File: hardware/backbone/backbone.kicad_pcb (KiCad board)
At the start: 4 copper layers, 31.3 x 68.9 mm, 113 parts, among them J1 RESET, J10 CORE_A, J11 MOUNT, J12 PW, J13 FIELD_B, J14 FIELD_A, J15 UART PROG, J16 ALED, J2 FROM_PREVIOUS, J4 FROM_PREVIOUS, J5 CONN_A, J6 BOOTLOADER, J7 CONN_B, J8 CORE_B, J9 TO NEXT, Q2 AO3401A, U11 470nH DCR=450m, U13 470nH DCR=450m, U15 ST25R100, U17 BLM18PG471SZ1D, U2 SN65HVD230DR, U4 AP2112K-3.3TRG1, U5 ESP32-C3-MINI-1-H4X, U8 G3VM-61VY3, U9 SN74AHCT1G14DCKR, X1 NX2016SA 27.12MHz

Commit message: fixed silkscreen
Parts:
- removed kobee-studio-6AA93B92: Kobee Studio, kobee-studio-6AA82ECF
- added kobee-studio-6AAAAB89: Kobee Studio, kobee-studio-6AA835EE, F.Cu at (177.9, 83.1)
- added kobee-studio-6AAAAB9F: Kobee Studio, kobee-studio-6AA835EE, F.Cu at (173.6, 83.5)
- moved kobee-studio-6AA93B19 17.8 mm to (167.4, 105.8), turned to 0 degrees
- moved kobee-studio-6AA93BB9 4.59 mm to (176.9, 123.6), turned to 90 degrees
- moved kobee-studio-6AAAAAAB 0.76 mm to (178.8, 112.3)
- moved kobee-studio-6AAAAAA1 0.41 mm to (178.8, 109.5)
- moved kobee-studio-6AAAAB45 0.27 mm to (156.4, 112.3)
- moved kobee-studio-6AA93B26 0.20 mm to (180.9, 88.0)
- moved kobee-studio-6AAAAA98 0.17 mm to (178.8, 106.7)
- moved kobee-studio-6AAAAB56 0.07 mm to (156.4, 109.2)
- renumbered kobee-studio-6AA83BBD to kobee-studio-6AAAAA98, kobee-studio-6AA83BE1 to kobee-studio-6AAAAAA1, kobee-studio-6AA83B6C to kobee-studio-6AAAAAAB, kobee-studio-6AA83B6C to kobee-studio-6AAAAB45, kobee-studio-6AA83B72 to kobee-studio-6AAAAB56

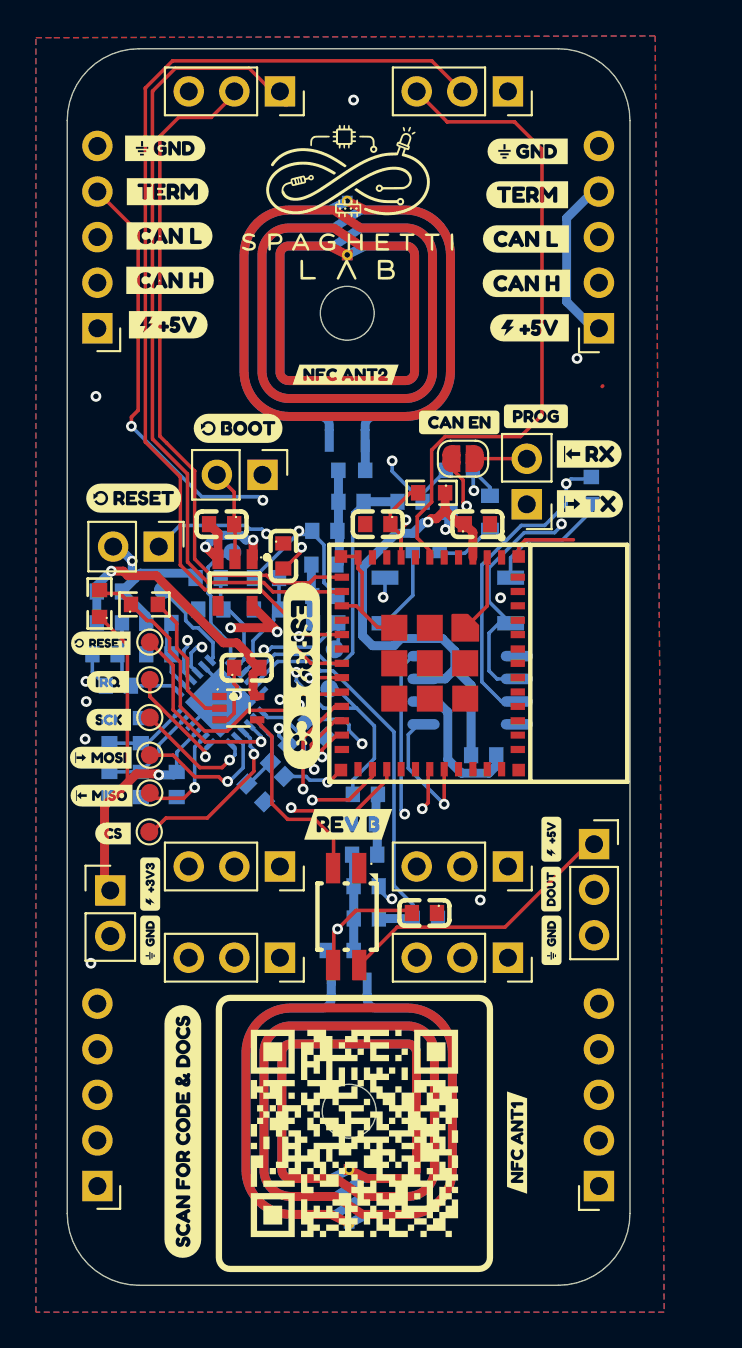
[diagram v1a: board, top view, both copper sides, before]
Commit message: added usb c to backbone, changed esp32 c3 to esp32 s3 so no more core needed to power the board and program it
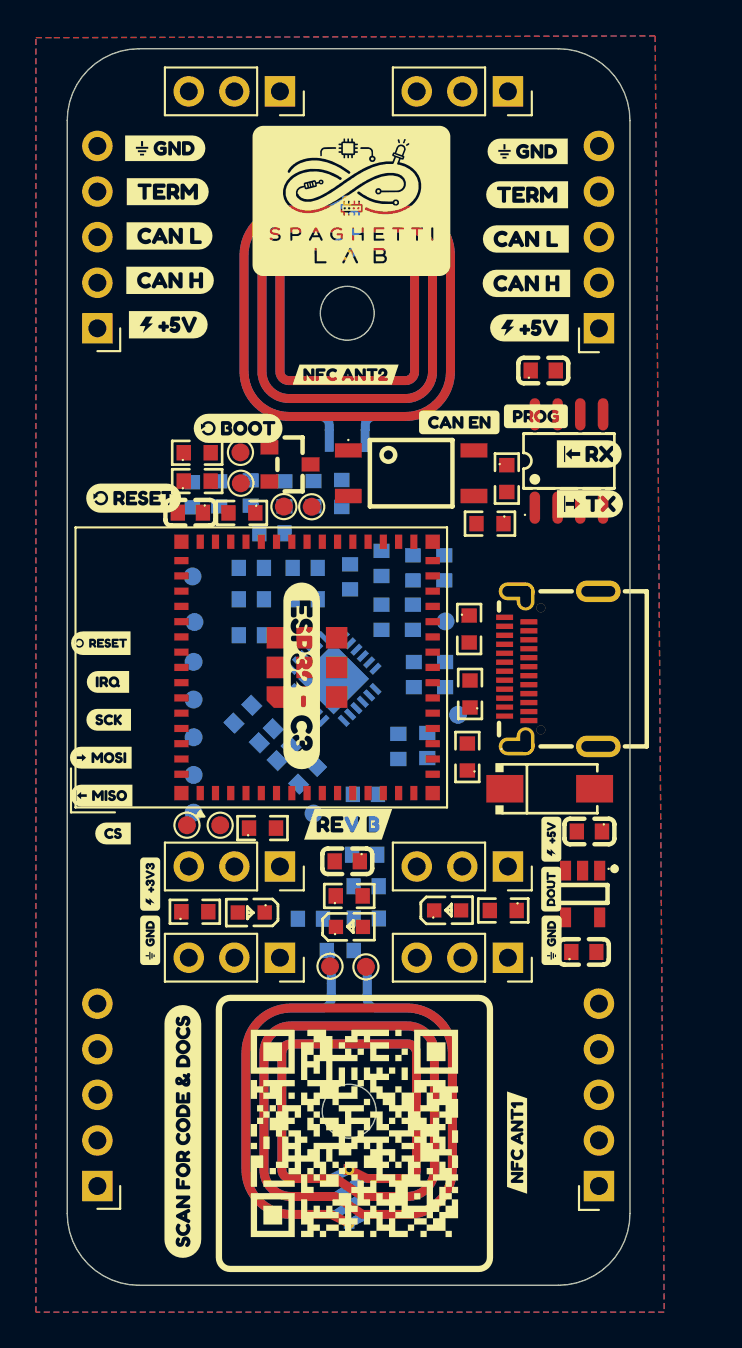
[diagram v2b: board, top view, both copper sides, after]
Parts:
- removed C12, C22, C3, C7: 100nF, SpaghettiLAB2:C0603
- removed J1: RESET, Connector_PinHeader_2.54mm:PinHeader_1x02_P2.54mm_Vertical
- removed J12: PW, Connector_PinHeader_2.54mm:PinHeader_1x02_P2.54mm_Vertical
- removed J15: UART PROG, Connector_PinHeader_2.54mm:PinHeader_1x02_P2.54mm_Vertical
- removed J16: ALED, Connector_PinSocket_2.54mm:PinSocket_1x03_P2.54mm_Vertical
- removed J6: BOOTLOADER, Connector_PinHeader_2.54mm:PinHeader_1x02_P2.54mm_Vertical
- removed JP1: FIRST_PROG, Jumper:SolderJumper-2_P1.3mm_Open_RoundedPad1.0x1.5mm
- removed LED1: SK6812MINI-E, SpaghettiLAB2:LED-SMD_4P-L3.2-W2.8-LS5.9_SK6812MINI-E
- removed R1, R2: 4.7k, SpaghettiLAB2:R0603
- removed R9: 220R, SpaghettiLAB2:R0603
- removed U5: ESP32-C3-MINI-1-H4X, SpaghettiLAB:WIFIM-SMD_ESP32-C3-MINI-1
- removed U9: SN74AHCT1G14DCKR, SpaghettiLAB2:SOT-353_L2.2-W1.4-P0.65-LS2.4-BR
- added C73: 100nF, SpaghettiLAB:C0603, F.Cu at (158.7, 88.5)
- added C74: 100nF, SpaghettiLAB:C0603, F.Cu at (167.4, 107.9)
- added D2: LED, SpaghettiLAB:LED0603-RD, F.Cu at (162.1, 110.8)
- added D3: LED, SpaghettiLAB:LED0603-RD, F.Cu at (173.0, 110.6)
- added D4: SS54_C22452, SpaghettiLAB:SMA_L4.4-W2.8-LS5.4-R-RD, F.Cu at (178.7, 103.9)
- added D5: LED, SpaghettiLAB:LED0603-RD, F.Cu at (167.5, 111.6)
- added R15: 4.7k, SpaghettiLAB:R0603, F.Cu at (162.7, 106.1)
- added R16: 4.7k, SpaghettiLAB:R0603, F.Cu at (161.5, 88.5)
- added R17: 33R, SpaghettiLAB:R0603, F.Cu at (174.2, 95.0)
- added R18: 33R, SpaghettiLAB:R0603, F.Cu at (174.2, 98.6)
- added R20: 5.1k, SpaghettiLAB:R0603, F.Cu at (175.3, 89.1)
- added R21: 330R, SpaghettiLAB:R0603, F.Cu at (158.9, 110.7)
- added R22: 330R, SpaghettiLAB:R0603, F.Cu at (176.1, 110.7)
- added R23: 5.1k, SpaghettiLAB:R0603, F.Cu at (174.1, 102.1)
- added R24: 330R, SpaghettiLAB:R0603, F.Cu at (167.5, 109.8)
- added TP12: SMD/0.6mm, TestPoint:TestPoint_Pad_D1.0mm, F.Cu at (160.3, 105.9)
- added TP13: SMD/0.6mm, TestPoint:TestPoint_Pad_D1.0mm, F.Cu at (161.4, 85.1)
- added TP15: SMD/0.6mm, TestPoint:TestPoint_Pad_D1.0mm, F.Cu at (166.4, 113.8)
- added TP18: SMD/0.6mm, TestPoint:TestPoint_Pad_D1.0mm, F.Cu at (163.9, 88.2)
- added TP19: SMD/0.6mm, TestPoint:TestPoint_Pad_D1.0mm, F.Cu at (165.4, 88.2)
- added TP21: SMD/0.6mm, TestPoint:TestPoint_Pad_D1.0mm, F.Cu at (168.4, 113.8)
- added TP8: SMD/0.6mm, TestPoint:TestPoint_Pad_D1.0mm, F.Cu at (161.5, 86.8)
- added TP9: SMD/0.6mm, TestPoint:TestPoint_Pad_D1.0mm, F.Cu at (158.5, 105.9)
- added U19: ESP32-S3-MINI-1, RF_Module:ESP32-S2-MINI-1, F.Cu at (162.6, 97.1)
- added USB1: TYPEC-324G-BCP24, SpaghettiLAB:USB-C-SMD_TYPEC-324G-BCP24, F.Cu at (178.8, 97.2)
- C1, Q2, R4, R5, R8, U2, U8: moved to F.Cu
- TP10, TP11, TP14, TP16, TP6, TP7: moved to B.Cu
- moved C9 27.7 mm to (180.6, 113.0), turned to 0 degrees
- moved C5 26.7 mm to (180.9, 106.2)
- moved U4 26.0 mm to (180.5, 109.7)
- moved C1 21.7 mm to (178.3, 80.6)
- moved C72 18.7 mm to (172.8, 91.6), turned to 90 degrees
- moved U17 17.2 mm to (171.1, 91.6), turned to 90 degrees
- moved C62 16.2 mm to (169.3, 91.3), turned to -90 degrees
- moved TP20 15.8 mm to (172.9, 94.5), turned to 90 degrees
- moved TP17 15.5 mm to (173.6, 99.8), turned to 90 degrees
- moved R4 14.6 mm to (159.0, 85.2)
- moved C33 14.4 mm to (162.1, 91.6), turned to 0 degrees
- moved C58 14.3 mm to (167.6, 92.1), turned to -90 degrees
- moved C39 14.2 mm to (165.1, 91.6), turned to 180 degrees
- moved C70 14.2 mm to (171.1, 94.3), turned to -90 degrees
- moved U2 13.9 mm to (179.8, 85.6), turned to 0 degrees
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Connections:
- net /RFI1_25R200 renamed /RFI1_25R100
- net /RFI2_25R200 renamed /RFI2_25R100
- net /RFO1_25R200 renamed /RFO1_25R100
- net /RFO2_25R200 renamed /RFO2_25R100
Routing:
- net VCORE: track 88.2 -> 0.00 mm, vias 5 -> 0
- net 5V: track 83.9 -> 0.00 mm, vias 5 -> 0
- net CAN_H: track 81.1 -> 0.00 mm, vias 1 -> 0
- net GND: track 76.5 -> 0.05 mm, vias 18 -> 0
- net CAN_L: track 73.1 -> 0.00 mm, vias 1 -> 0
- net A3: track 58.4 -> 0.00 mm
- net A1: track 45.2 -> 0.00 mm
- net A0: track 38.5 -> 0.00 mm
- net TERM_CTRL_OUT: track 38.4 -> 0.00 mm, vias 3 -> 0
- net A2: track 36.8 -> 0.00 mm
- net CAN_RX: track 31.9 -> 0.00 mm, vias 2 -> 0
- net Net-(J15-Pin_2): track 28.5 -> 0.00 mm, vias 1 -> 0
- net CAN_TX: track 28.1 -> 0.00 mm, vias 1 -> 0
- net LED_DATA/STRAP: track 24.6 -> 0.00 mm, vias 2 -> 0
- net IO9/BOOT: track 23.4 -> 0.00 mm, vias 1 -> 0
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
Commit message: board with usb and esp32 s3 completely routed
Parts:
- removed TP10, TP11, TP14, TP16, TP6, TP7: SMD/0.6mm, TestPoint:TestPoint_Pad_D1.0mm
- removed kobee-studio-6AA834E9: Kobee Studio, kobee-studio-6AA834DA
- removed kobee-studio-6AA83AC8, kobee-studio-6AA93B33, kobee-studio-6AA93C2C: Kobee Studio, kobee-studio-6AA82ECF
- removed kobee-studio-6AA93ACC, kobee-studio-6AAAAAA1, kobee-studio-6AAAAB45, kobee-studio-6AAAAB89, kobee-studio-6AAAAB9F: Kobee Studio, kobee-studio-6AA835EE
- removed kobee-studio-6AA93B20, kobee-studio-6AA93B26: Kobee Studio, kobee-studio-6AA82B88
- removed kobee-studio-6AA93B3B, kobee-studio-6AA93B41: Kobee Studio, kobee-studio-6AA82E83
- removed kobee-studio-6AA93B49: Kobee Studio, kobee-studio-6AA82EBC
- removed kobee-studio-6AA93B50: Kobee Studio, kobee-studio-6AA82E9A
- removed kobee-studio-6AA93B59: Kobee Studio, kobee-studio-6AA82E4A
- removed kobee-studio-6AAAAA98, kobee-studio-6AAAAB56: Kobee Studio, kobee-studio-6AA83B2B
- added kobee-studio-6AA93B08: Kobee Studio, kobee-studio-6AA835EE, F.Cu at (177.4, 68.2)
- moved TP13 36.5 mm to (178.2, 117.5)
- moved TP12 22.2 mm to (175.1, 89.3)
- moved R20 17.0 mm to (178.0, 105.9)
- moved kobee-studio-6AA93B19 14.2 mm to (154.0, 110.4), turned to 90 degrees
- moved TP4 11.6 mm to (170.2, 94.3)
- moved U13 11.2 mm to (167.5, 94.6), turned to 180 degrees
- moved TP9 10.3 mm to (168.8, 106.0)
- moved C1 10.2 mm to (179.7, 90.6), turned to 180 degrees
- moved C72 9.86 mm to (163.1, 89.8), turned to 180 degrees
- moved C16 9.05 mm to (167.5, 92.8), turned to 0 degrees
- moved kobee-studio-6AAAAAAB 8.04 mm to (186.8, 112.4)
- moved U17 7.95 mm to (163.1, 91.3), turned to 180 degrees
- moved C48 7.42 mm to (170.4, 88.0), turned to 180 degrees
- moved C62 6.91 mm to (163.1, 94.2), turned to 0 degrees
- moved C28 6.72 mm to (167.5, 91.3), turned to 0 degrees
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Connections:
- Q2 pad 2: Net-(Q2-S) -> 5V
- Q2 pad 3: 5V -> Net-(Q2-D)
- R5 pad 2: Net-(Q2-S) -> Net-(Q2-D)
- U19 pad 10: unconnected-(U19-IO6-Pad10) -> NFC_MISO
- U19 pad 11: unconnected-(U19-IO7-Pad11) -> IO7
- U19 pad 12: unconnected-(U19-IO8-Pad12) -> IO8
- U19 pad 13: unconnected-(U19-IO9-Pad13) -> IO9
- U19 pad 14: IO10 -> STATUS
- U19 pad 29: STATUS -> CAN_RX
- U19 pad 30: IO48 -> CAN_TX
- U19 pad 31: IO35 -> A3
- U19 pad 32: IO36 -> A2
- U19 pad 33: IO37 -> A1
- U19 pad 34: IO38 -> A0
- U19 pad 5: IO1 -> NFC_RST
- U19 pad 6: IO2 -> NFC_CS
- U19 pad 7: IO3 -> NFC_MOSI
- U19 pad 8: CAN_RX -> NFC_SCK
- U19 pad 9: CAN_TX -> NFC_IRQ
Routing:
- net 5V: track 0.00 -> 106.6 mm, vias 0 -> 2
- net VCORE: track 0.00 -> 96.5 mm, vias 0 -> 5
- net GND: track 0.05 -> 87.8 mm, vias 0 -> 21
- net CAN_L: track 0.00 -> 55.0 mm
- net CAN_H: track 0.00 -> 55.0 mm
- net A0: track 0.00 -> 44.6 mm, vias 0 -> 1
- net A1: track 0.00 -> 42.3 mm, vias 0 -> 1
- net A2: track 0.00 -> 34.9 mm, vias 0 -> 1
- net /RFI1_25R100: track 0.00 -> 34.5 mm, vias 0 -> 2
- net A3: track 0.00 -> 32.5 mm, vias 0 -> 1
- net VBUS: track 0.00 -> 26.4 mm, vias 0 -> 5
- net TERM_CTRL_OUT: track 0.00 -> 22.6 mm
- net /RFO2_25R100: track 0.00 -> 20.8 mm
- net USB_D-: track 0.00 -> 15.5 mm, vias 0 -> 3
- net USB_D+: track 0.00 -> 14.7 mm, vias 0 -> 3
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
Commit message: fix backbone schematic connectivity and power flags
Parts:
- C1, C13, C16, C18, C20, C23, C28, C30, C32, C33, C35, C37, C39, C41, C43, C46, C48, C5, C51, C54, C55, C58, C60, C62, C63, C65, C70, C72, C9: footprint SpaghettiLAB2:C0603 -> SpaghettiLAB:C0603
- R11, R14, R4, R5, R8: footprint SpaghettiLAB2:R0603 -> SpaghettiLAB:R0603
- U4: footprint SpaghettiLAB2:SOT-25-5_L2.9-W1.6-P0.95-LS2.8-BL -> SpaghettiLAB:SOT-25-5_L2.9-W1.6-P0.95-LS2.8-BL
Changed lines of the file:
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@@
 		(embedded_fonts no)
 	)
-	(footprint "SpaghettiLAB2:C0603"
+	(footprint "SpaghettiLAB:C0603"
 		(layer "F.Cu")
 		(at 180.63 112.81)
@@
 		(embedded_fonts no)
 	)
-	(footprint "SpaghettiLAB2:C0603"
+	(footprint "SpaghettiLAB:C0603"
 		(layer "F.Cu")
 		(at 179.73 90.63 180)
@@
 		)
 	)
-	(footprint "SpaghettiLAB2:R0603"
+	(footprint "SpaghettiLAB:R0603"
 		(layer "F.Cu")
 		(at 159.09 86.58)
@@
 		(embedded_fonts no)
 	)
-	(footprint "SpaghettiLAB2:SOT-25-5_L2.9-W1.6-P0.95-LS2.8-BL"
+	(footprint "SpaghettiLAB:SOT-25-5_L2.9-W1.6-P0.95-LS2.8-BL"
 		(layer "F.Cu")
 		(at 180.56 109.58 180)
@@
 		(embedded_fonts no)
 	)
-	(footprint "SpaghettiLAB2:C0603"
+	(footprint "SpaghettiLAB:C0603"
 		(layer "F.Cu")
 		(at 180.94 106.1 180)
@@
 		)
 	)
-	(footprint "SpaghettiLAB2:R0603"
+	(footprint "SpaghettiLAB:R0603"
 		(layer "F.Cu")
 		(at 176.34 86.44 -90)
@@
 		(embedded_fonts no)
 	)
-	(footprint "SpaghettiLAB2:R0603"
+	(footprint "SpaghettiLAB:R0603"
 		(layer "F.Cu")
 		(at 159.32 85)
@@
 		)
 	)
-	(footprint "SpaghettiLAB2:C0603"
+	(footprint "SpaghettiLAB:C0603"
 		(layer "B.Cu")
 		(at 170.45 88.02 180)
@@
 		)
 	)
-	(footprint "SpaghettiLAB2:R0603"
+	(footprint "SpaghettiLAB:R0603"
 		(layer "B.Cu")
 		(at 167.368898 86.464408)
@@
 		)
 	)
-	(footprint "SpaghettiLAB2:C0603"
+	(footprint "SpaghettiLAB:C0603"
 		(layer "B.Cu")
 		(at 170.11 98.7 -90)
@@
 		)
 	)
-	(footprint "SpaghettiLAB2:R0603"
+	(footprint "SpaghettiLAB:R0603"
 		(layer "B.Cu")
 		(at 167.42 112.88 180)
@@
 		)
 	)
-	(footprint "SpaghettiLAB2:C0603"
+	(footprint "SpaghettiLAB:C0603"
 		(layer "B.Cu")
 		(at 158.12 94.37 -90)
@@
 		)
 	)
-	(footprint "SpaghettiLAB2:C0603"
+	(footprint "SpaghettiLAB:C0603"
 		(layer "B.Cu")
 		(at 160.89 91.89 -90)
@@
 		(embedded_fonts no)
 	)
-	(footprint "SpaghettiLAB2:C0603"
+	(footprint "SpaghettiLAB:C0603"
 		(layer "B.Cu")
 		(at 167.38 89.666645 180)
@@
 		)
 	)
-	(footprint "SpaghettiLAB2:C0603"
+	(footprint "SpaghettiLAB:C0603"
 		(layer "B.Cu")
 		(at 167.46 107.868 180)
@@
 		(embedded_fonts no)
 	)
-	(footprint "SpaghettiLAB2:C0603"
+	(footprint "SpaghettiLAB:C0603"
 		(layer "B.Cu")
 		(at 162.79 105.29 -135)
@@
 		)
 	)
-	(footprint "SpaghettiLAB2:C0603"
+	(footprint "SpaghettiLAB:C0603"
 		(layer "B.Cu")
 		(at 165.26 93.78 -90)
@@
 		(embedded_fonts no)
 	)
-	(footprint "SpaghettiLAB2:C0603"
+	(footprint "SpaghettiLAB:C0603"
 		(layer "B.Cu")
 		(at 167.52 92.85)
@@
 		)
 	)
-	(footprint "SpaghettiLAB2:C0603"
+	(footprint "SpaghettiLAB:C0603"
 		(layer "B.Cu")
 		(at 167.44 111.276 180)
@@
 		)
 	)
-	(footprint "SpaghettiLAB2:C0603"
+	(footprint "SpaghettiLAB:C0603"
 		(layer "B.Cu")
 		(at 168.12 101.9 90)
@@
 		)
 	)
-	(footprint "SpaghettiLAB2:C0603"
+	(footprint "SpaghettiLAB:C0603"
 		(layer "B.Cu")
 		(at 164.31 110.83 180)
@@
 		)
 	)
-	(footprint "SpaghettiLAB2:C0603"
+	(footprint "SpaghettiLAB:C0603"
 		(layer "B.Cu")
 		(at 167.46 109.572 180)
@@
 		)
 	)
-	(footprint "SpaghettiLAB2:C0603"
+	(footprint "SpaghettiLAB:C0603"
 		(layer "B.Cu")
 		(at 163.09 92.69)
@@
 		)
 	)
-	(footprint "SpaghettiLAB2:C0603"
+	(footprint "SpaghettiLAB:C0603"
 		(layer "B.Cu")
 		(at 159.1 101.98 45)
@@
 		)
 	)
-	(footprint "SpaghettiLAB2:C0603"
+	(footprint "SpaghettiLAB:C0603"
 		(layer "B.Cu")
 		(at 167.38 88.015526 180)
@@
 		)
 	)
-	(footprint "SpaghettiLAB2:C0603"
+	(footprint "SpaghettiLAB:C0603"
 		(layer "B.Cu")
 		(at 158.88 97.14)
@@
 		(embedded_fonts no)
 	)
-	(footprint "SpaghettiLAB2:C0603"
+	(footprint "SpaghettiLAB:C0603"
 		(layer "B.Cu")
 		(at 159.58 94.34 -90)
@@
 		)
 	)
-	(footprint "SpaghettiLAB2:C0603"
+	(footprint "SpaghettiLAB:C0603"
 		(layer "B.Cu")
 		(at 168.42 98.7 -90)
@@
 		)
 	)
-	(footprint "SpaghettiLAB2:C0603"
+	(footprint "SpaghettiLAB:C0603"
 		(layer "B.Cu")
 		(at 167.47 106.164)
@@
 		)
 	)
-	(footprint "SpaghettiLAB2:C0603"
+	(footprint "SpaghettiLAB:C0603"
 		(layer "B.Cu")
 		(at 161.1 94.66 -90)
@@
 		)
 	)
-	(footprint "SpaghettiLAB2:C0603"
+	(footprint "SpaghettiLAB:C0603"
 		(layer "B.Cu")
 		(at 169.65 101.85 90)
@@
 		(embedded_fonts no)
 	)
-	(footprint "SpaghettiLAB2:C0603"
+	(footprint "SpaghettiLAB:C0603"
 		(layer "B.Cu")
 		(at 167.47 91.317763)
@@
 		)
 	)
-	(footprint "SpaghettiLAB2:C0603"
+	(footprint "SpaghettiLAB:C0603"
 		(layer "B.Cu")
 		(at 163.11 89.8 180)
@@
 		)
 	)
-	(footprint "SpaghettiLAB2:C0603"
+	(footprint "SpaghettiLAB:C0603"
 		(layer "B.Cu")
 		(at 163.05 94.24)
@@
 		)
 	)
-	(footprint "SpaghettiLAB2:C0603"
+	(footprint "SpaghettiLAB:C0603"
 		(layer "B.Cu")
 		(at 165.24 91 -90)
